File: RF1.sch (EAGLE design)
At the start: 15 parts, among them J1 5v, Q1 16mhz, U1 ATMEGA328P_PDIP

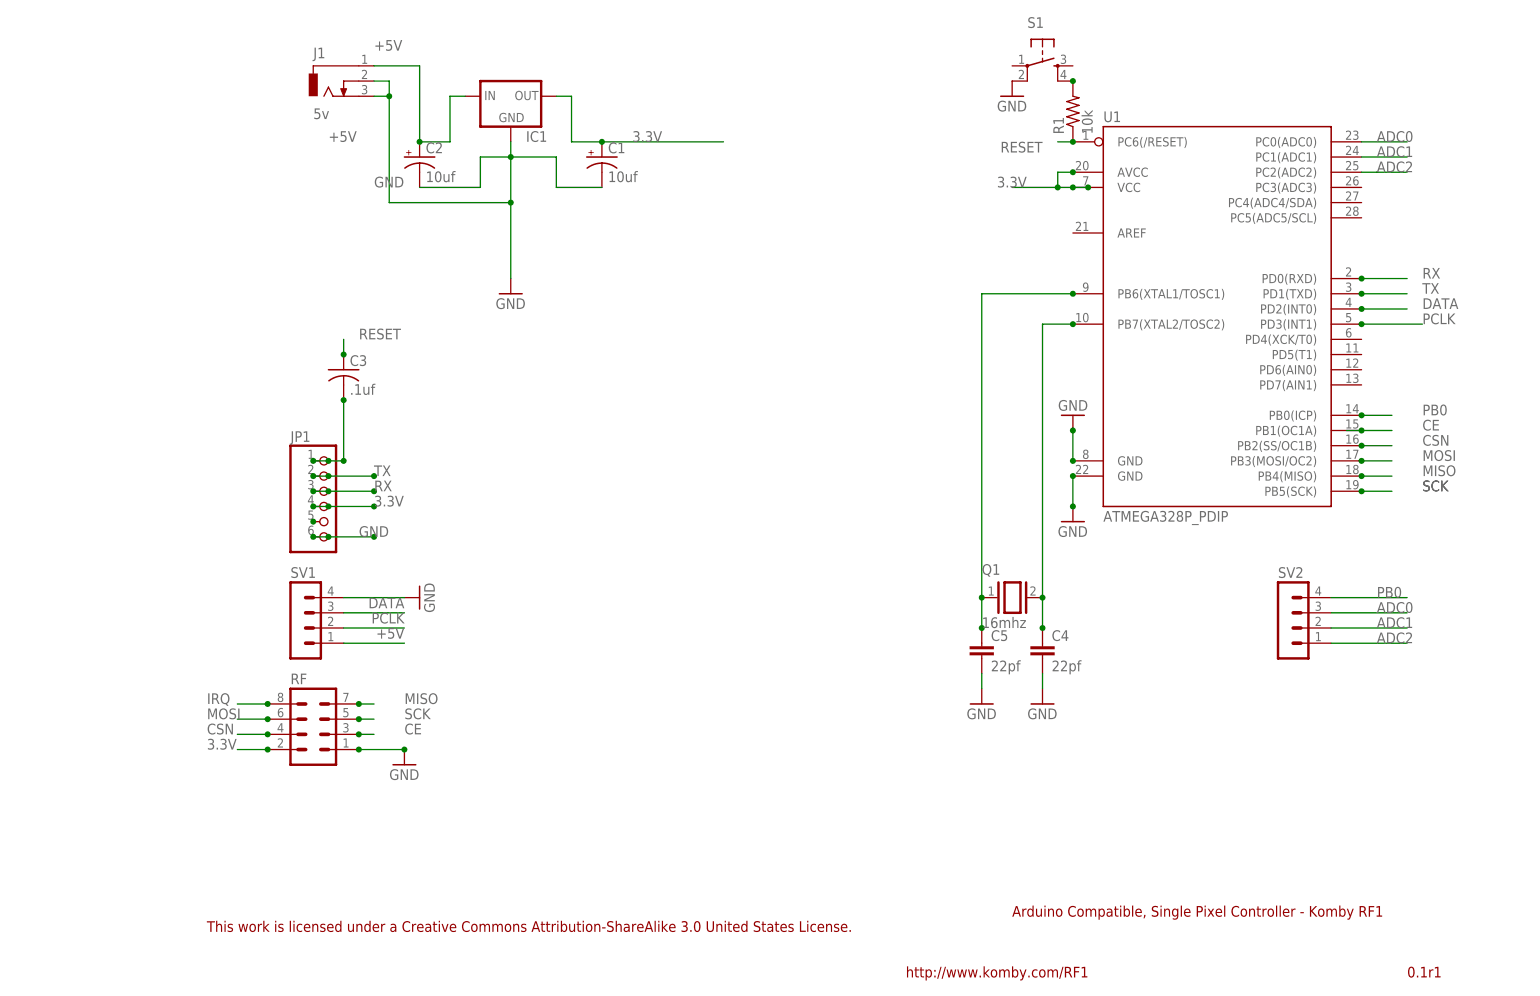
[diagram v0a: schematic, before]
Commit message: Updated Revised layout of RF1 board
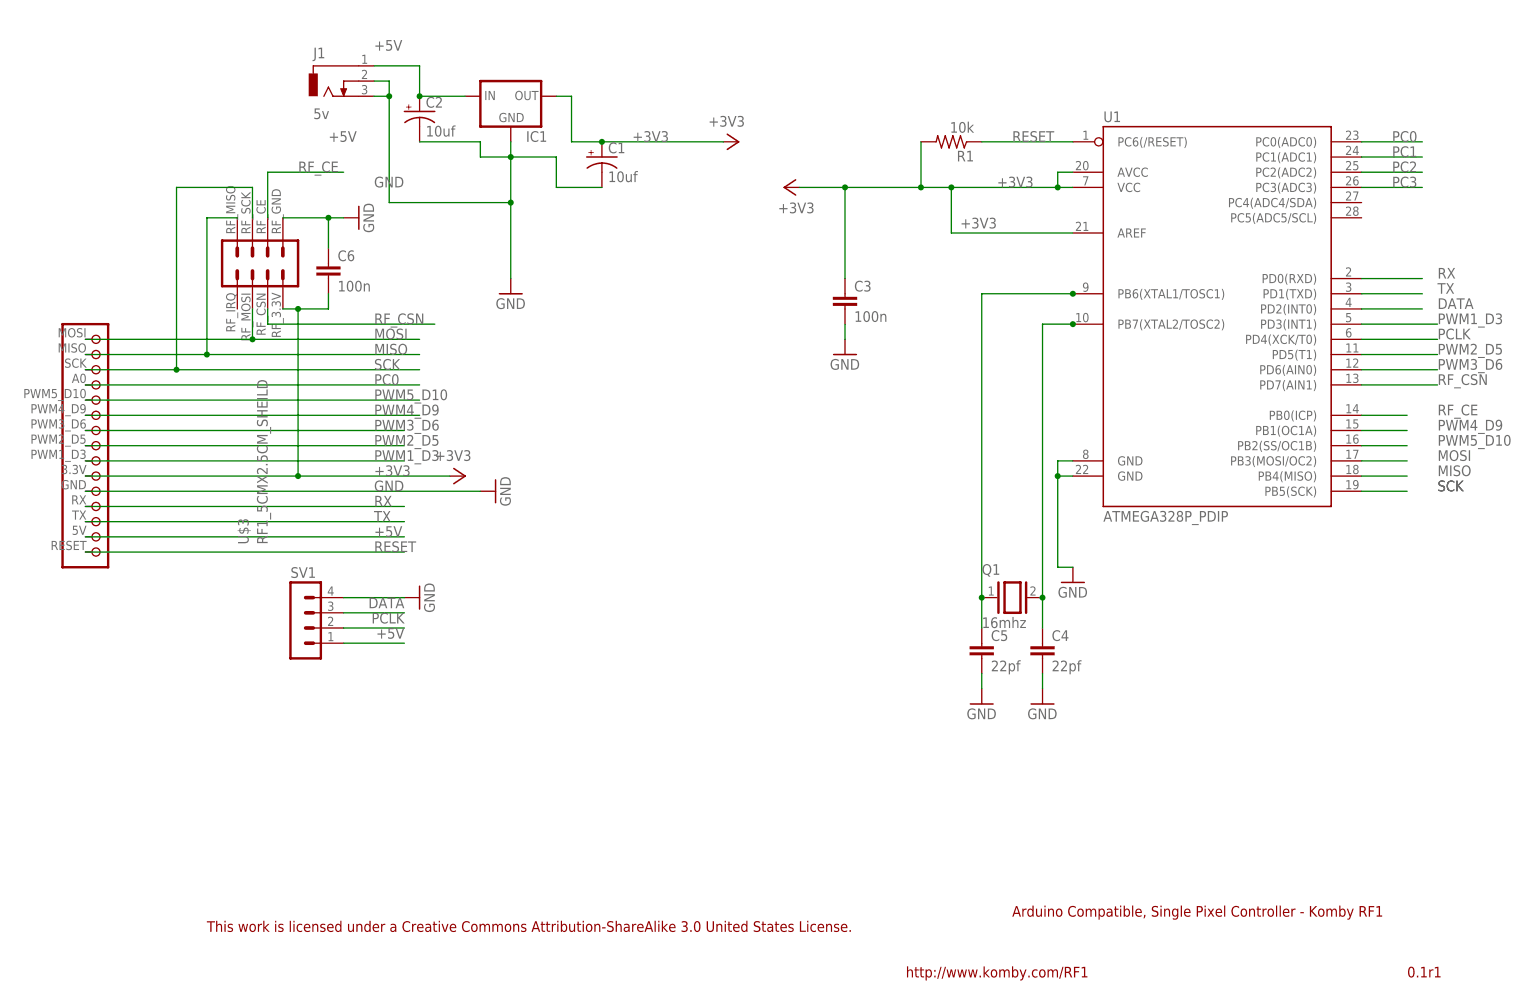
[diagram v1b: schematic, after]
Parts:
- removed JP1: (no value), adafruit:PINHD-1X6B
- removed RF: (no value), con-lstb:MA04-2
- removed S1: (no value), SparkFun-Electromechanical:TAC_SWITCHPTH
- removed SV2: (no value), con-lstb:MA04-1
- added C6: 100n, resistor:C-EU025-024X044
- added U$3: RF1_5CMX2.5CM_SHEILD, komby1:RF1_5CMX2.5CM_SHEILD
- C3: value .1uf -> 100n; device adafruit:C-US025-024X044 -> resistor:C-EU025-024X044
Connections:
- removed net 3.3V: C1.+, IC1.OUT, JP1.4, RF.2, U1.AVCC, U1.VCC
- removed net ADC0: SV2.3, U1.PC0(ADC0)
- removed net ADC1: SV2.2, U1.PC1(ADC1)
- removed net ADC2: SV2.1, U1.PC2(ADC2)
- removed net CE: RF.3, U1.PB1(OC1A)
- removed net CSN: RF.4, U1.PB2(SS/OC1B)
- removed net IRQ: RF.8
- removed net N$1: R1.2, S1.4
- removed net N$7: C3.2, JP1.1
- removed net N$8: JP1.5
- removed net PB0: SV2.4, U1.PB0(ICP)
- new net +3V3: C1.+, C3.1, C6.2, IC1.OUT, R1.2, U$3.3.3V, U$3.RF_3.3V, U1.AREF, U1.AVCC, U1.VCC
- new net PC0: U$3.PC0, U1.PC0(ADC0)
- new net PC1: U1.PC1(ADC1)
- new net PC2: U1.PC2(ADC2)
- new net PC3: U1.PC3(ADC3)
- new net PWM1_D3: U$3.PWM1, U1.PD3(INT1)
- new net PWM2_D5: U$3.PWM2, U1.PD5(T1)
- new net PWM3_D6: U$3.PWM3, U1.PD6(AIN0)
- new net PWM4_D9: U$3.PWM4, U1.PB1(OC1A)
- new net PWM5_D10: U$3.PWM5, U1.PB2(SS/OC1B)
- new net RF_CE: U$3.RF_CE, U1.PB0(ICP)
- new net RF_CSN: U$3.RF_CSN, U1.PD7(AIN1)
- net +5V: now also U$3.5V
- net GND: now also C3.2, C6.1, U$3.GND, U$3.RFGND_1; no longer JP1.6, RF.1, S1.2
- net MISO: now also U$3.MISO, U$3.RF_MISO; no longer RF.7
- net MOSI: now also U$3.MOSI, U$3.RF_MOSI; no longer RF.6
- net PCLK: now also U1.PD4(XCK/T0); no longer U1.PD3(INT1)
- net RESET: now also U$3.RESET; no longer C3.1
- net RX: now also U$3.RX; no longer JP1.3
- net SCK: now also U$3.RF_SCK, U$3.SCK; no longer RF.5
- net TX: now also U$3.TX; no longer JP1.2
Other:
- moved on the sheet: C2, C3, R1
